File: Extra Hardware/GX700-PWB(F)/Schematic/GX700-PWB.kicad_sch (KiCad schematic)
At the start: 85 parts

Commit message: A lot of fixes.
Moved some libraries about to allow other schematics to share parts. 573 Expansion IO now has a proper symbol and part. JAE TX15 connector has a footprint. GX700 IO board has been fixed (output from chips was entirely wrong).
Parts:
- added CN31, CN32: 573_EXP, Connectors:JAE-TX15-80P, symbol Konami:573_EXP
- added H? (x3): MountingHole_Pad, symbol Mechanical:MountingHole_Pad
- added H?: MountingHole, symbol Mechanical:MountingHole
- added JP? (x3): Jumper_2_Open, symbol Jumper:Jumper_2_Open
- added RA2: 4.7k, Resistor_THT:R_Array_SIP9, symbol Device:R_Network08
- 10H: value (none) -> GAL16V8 (X700F1); footprint (none) -> Package_DIP:DIP-20_W7.62mm
- 3A: renamed from 6T?; value (none) -> PC817; footprint (none) -> Package_DIP:DIP-4_W7.62mm
- 3B: renamed from 6U?; value (none) -> PC817; footprint (none) -> Package_DIP:DIP-4_W7.62mm
- 3C: renamed from 6V?; value (none) -> PC817; footprint (none) -> Package_DIP:DIP-4_W7.62mm
- 3D: renamed from 6W?; value (none) -> PC817; footprint (none) -> Package_DIP:DIP-4_W7.62mm
- 3E, 3F, 3G, 3H, 3J, 3K, 3L, 3M, 3P, 3Q, 3R, 3S, 3T, 3U, 3V, 3W, 6T, 6U, 6V, 6W, 6X, 6Y, 6Z: value (none) -> PC817; footprint (none) -> Package_DIP:DIP-4_W7.62mm
- C17, C19, C6, C7, C8: value (none) -> 1uf; footprint (none) -> Capacitor_THT:C_Axial_L3.8mm_D2.6mm_P10.00mm_Horizontal
- C8: value (none) -> 1uf; footprint (none) -> 1uf
- CN33, CN34, CN35: value (none) -> B10PSHF1A; footprint (none) -> Connector_JST:JST_NH_B10P_SHD
- CN36: renamed from J?; value (none) -> B6PSHF1AA
- FL? (x28): value (none) -> EMI_Filter_LCL; footprint (none) -> Connector_PinSocket_2.54mm:PinSocket_1x03_P2.54mm_Vertical
- FL? (x4): value (none) -> EMI_Filter_LCL
- R11, R12, R13, R14: value (none) -> 4.7k; footprint (none) -> Resistor_THT:R_Axial_DIN0204_L3.6mm_D1.6mm_P5.08mm_Horizontal
- RA3: value (none) -> 4.7k; footprint (none) -> Resistor_THT:R_Array_SIP9
- RA4, RA5, RA?, RN6: value (none) -> 470; footprint (none) -> Resistor_THT:R_Array_SIP9
- U14, U3, U34: value (none) -> 74LS273; footprint (none) -> Package_DIP:DIP-20_W7.62mm
- U9: value (none) -> 74LS175; footprint (none) -> Package_DIP:DIP-16_W7.62mm
- U?: value (none) -> 74LS244
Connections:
- net +5V: now also CN31.a1 (+5V), CN31.a2 (+5V), CN31.a3 (+5V), CN31.a4 (+5V), CN31.a5 (+5V), CN31.b1 (+5V), CN31.b2 (+5V), CN31.b3 (+5V), CN31.b4 (+5V), CN31.b5 (+5V), CN32.a1 (+5V), CN32.a2 (+5V), CN32.a3 (+5V), CN32.a4 (+5V), CN32.a5 (+5V), CN32.b1 (+5V), CN32.b2 (+5V), CN32.b3 (+5V), CN32.b4 (+5V), CN32.b5 (+5V)
- net 573-D0: now also RA3.2 (R1), U?.17 (I3b), CN31.a32 (D0), CN32.a32 (D0); no longer RA3.9 (R8), U?.2 (I0a)
- net 573-D1: now also RA3.3 (R2), U?.15 (I2b), CN31.b32 (D1), CN32.b32 (D1); no longer RA3.8 (R7), U?.4 (I1a)
- net 573-D2: now also RA3.4 (R3), U?.13 (I1b), CN31.a31 (D2), CN32.a31 (D2); no longer RA3.7 (R6), U?.6 (I2a)
- net 573-D3: now also RA3.5 (R4), U?.11 (I0b), CN31.b31 (D3), CN32.b31 (D3); no longer RA3.6 (R5), U?.8 (I3a)
- net 573-D4: now also RA3.6 (R5), U?.8 (I3a), CN31.a30 (D4), CN32.a30 (D4); no longer RA3.5 (R4), U?.11 (I0b)
- net 573-D5: now also RA3.7 (R6), U?.6 (I2a), CN31.b30 (D5), CN32.b30 (D5); no longer RA3.4 (R3), U?.13 (I1b)
- net 573-D6: now also RA3.8 (R7), U?.4 (I1a), CN31.a29 (D6), CN32.a29 (D6); no longer RA3.3 (R2), U?.15 (I2b)
- net 573-D7: now also RA3.9 (R8), U?.2 (I0a), CN31.b29 (D7), CN32.b29 (D7); no longer RA3.2 (R1), U?.17 (I3b)
- net DATA-0: now also U?.3 (O3b); no longer U?.18 (O0a)
- net DATA-1: now also U?.5 (O2b); no longer U?.16 (O1a)
- net DATA-2: now also U?.7 (O1b); no longer U?.14 (O2a)
- net DATA-3: now also U?.9 (O0b); no longer U?.12 (O3a)
- net DATA-4: now also U?.12 (O3a); no longer U?.9 (O0b)
- net DATA-5: now also U?.14 (O2a); no longer U?.7 (O1b)
- net DATA-6: now also U?.16 (O1a); no longer U?.5 (O2b)
- net DATA-7: now also U?.18 (O0a); no longer U?.3 (O3b)
- net GND: now also CN31.a11 (GND), CN31.a13 (GND), CN31.a33 (GND), CN31.a34 (GND), CN31.a35 (GND), CN31.a8 (GND), CN31.a9 (GND), CN31.b11 (GND), CN31.b13 (GND), CN31.b33 (GND), CN31.b34 (GND), CN31.b35 (GND), CN31.b7 (GND), CN31.b9 (GND), CN32.a11 (GND), CN32.a13 (GND), CN32.a33 (GND), CN32.a34 (GND), CN32.a35 (GND), CN32.a8 (GND), CN32.a9 (GND), CN32.b11 (GND), CN32.b13 (GND), CN32.b33 (GND), CN32.b34 (GND), CN32.b35 (GND), CN32.b7 (GND), CN32.b9 (GND), JP?.1 (A), JP?.1 (A)
- net ISOLATED-COMMON: now also CN35.10 (Pin_10), CN36.6 (Pin_6), JP?.1 (A)
- net U14-CP: now also 10H.14 (IO6); no longer 10H.13 (IO7)
- net U3-CP: now also 10H.13 (IO7); no longer 10H.12 (IO8)
- net U34-CP: now also 10H.15 (IO5); no longer 10H.14 (IO6)
- net U9-CP: now also 10H.16 (IO4); no longer 10H.15 (IO5)
- net ~{RESET}: now also CN31.a10 (~{RESET}), CN32.a10 (~{RESET})
- net at U9.10 (Q2): now also 3B.2; no longer 3C.2
- net at U9.15 (Q3): now also 3A.2; no longer 3D.2
- net at U9.2 (Q0): now also 3D.2; no longer 3A.2
- net at U9.7 (Q1): now also 3C.2; no longer 3B.2
- net ~{EXP2}: now reaches 10H.1 (I1/CLK), R12.1
- net ~{EXP2}: now also CN31.a15 (~{EXP2}), CN32.a15 (~{EXP2})
- net ~{READ}: now reaches 10H.2 (I2), R14.1
- net ~{READ}: now also CN31.a6 (~{READ}), CN32.a6 (~{READ})
- net ~{WR1}: now reaches 10H.3 (I3), R11.1
- net ~{WR1}: now also CN31.b6 (~{WR1}), CN32.b6 (~{WR1})
- net at 3E.2: now also U34.19 (Q7); no longer U34.2 (Q0)
- net at CN35.1 (Pin_1), FL?.3: no longer CN35.10 (Pin_10)
- net at CN36.1 (Pin_1), FL?.3: no longer CN36.6 (Pin_6)
- net at U34.12 (Q4): now also 3L.2; no longer 3J.2
- net at U34.15 (Q5): now also 3J.2; no longer 3K.2
- net at U34.16 (Q6): now also 3G.2; no longer 3L.2
- net at 3M.2: now also U34.9 (Q3); no longer U34.19 (Q7)
- net at 3F.2: now also U34.2 (Q0); no longer U34.5 (Q1)
- net at U34.6 (Q2): now also 3K.2; no longer 3G.2
- net at 3H.2: now also U34.5 (Q1); no longer U34.9 (Q3)
- net at 3P.2: now also U14.19 (Q7); no longer U14.2 (Q0)
- net at U14.12 (Q4): now also 3V.2; no longer 3T.2
- net at U14.15 (Q5): now also 3T.2; no longer 3U.2
- net at U14.16 (Q6): now also 3R.2; no longer 3V.2
- net at 3W.2: now also U14.9 (Q3); no longer U14.19 (Q7)
- net at 3Q.2: now also U14.2 (Q0); no longer U14.5 (Q1)
- net at U14.6 (Q2): now also 3U.2; no longer 3R.2
- net at 3S.2: now also U14.5 (Q1); no longer U14.9 (Q3)
- net at 6T.2: now also U3.19 (Q7); no longer U3.2 (Q0)
- net at U3.12 (Q4): now also 6Y.2; no longer 6X.2
- net at U3.15 (Q5): now also 6X.2; no longer 6Y.2
- net at U3.16 (Q6): now also 6V.2; no longer 6Y.2
- net at 6Z.2: now also U3.9 (Q3); no longer U3.19 (Q7)
- net at 6U.2: now also U3.2 (Q0); no longer U3.5 (Q1)
- net at U3.6 (Q2): now also 6Y.2; no longer 6V.2
- net at 6W.2: now also U3.5 (Q1); no longer U3.9 (Q3)
- net 573-3V3 renamed +3V3
- net +3V3: now also CN31.a36 (+3V3), CN31.a37 (+3V3), CN31.a38 (+3V3), CN31.a39 (+3V3), CN31.a40 (+3V3), CN31.b36 (+3V3), CN31.b37 (+3V3), CN31.b38 (+3V3), CN31.b39 (+3V3), CN31.b40 (+3V3), CN32.a36 (+3V3), CN32.a37 (+3V3), CN32.a38 (+3V3), CN32.a39 (+3V3), CN32.a40 (+3V3), CN32.b36 (+3V3), CN32.b37 (+3V3), CN32.b38 (+3V3), CN32.b39 (+3V3), CN32.b40 (+3V3), RA2.1 (common)
- removed net 573-A??: 10H.5 (I5), 10H.6 (I6), 10H.7 (I7), 10H.8 (I8), 10H.9 (I9)
- new net: H?.1, JP?.2 (B) (x3)
- new net 573-A0: CN31.a24 (A0), CN32.a24 (A0)
- new net 573-A1: CN31.b24 (A1), CN32.b24 (A1)
- new net 573-A12: CN31.a20 (A12), CN32.a20 (A12)
- new net 573-A13: CN31.b20 (A13), CN32.b20 (A13)
- new net 573-A14: CN31.a19 (A14), CN32.a19 (A14)
- new net 573-A15: CN31.b19 (A15), CN32.b19 (A15)
- new net 573-A2: CN31.a23 (A2), CN32.a23 (A2)
- new net 573-A20: CN31.a18 (A20), CN32.a18 (A20)
- new net 573-A21: CN31.b18 (A21), CN32.b18 (A21)
- new net 573-A22: CN31.a17 (A22), CN32.a17 (A22)
- new net 573-A23: CN31.b17 (A23), CN32.b17 (A23)
- new net 573-A3: 10H.9 (I9), CN31.b23 (A3), CN32.b23 (A3), RA2.2 (R1)
- new net 573-A4: 10H.8 (I8), CN31.a22 (A4), CN32.a22 (A4), RA2.3 (R2)
- new net 573-A5: 10H.7 (I7), CN31.b22 (A5), CN32.b22 (A5), RA2.4 (R3)
- new net 573-A6: 10H.6 (I6), CN31.a21 (A6), CN32.a21 (A6), RA2.5 (R4)
- new net 573-A7: 10H.5 (I5), CN31.b21 (A7), CN32.b21 (A7), RA2.6 (R5)
- new net 573-D10: CN31.a27 (D10), CN32.a27 (D10)
- new net 573-D11: CN31.b27 (D11), CN32.b27 (D11)
- new net 573-D12: CN31.a26 (D12), CN32.a26 (D12)
- new net 573-D13: CN31.b26 (D13), CN32.b26 (D13)
- new net 573-D14: CN31.a25 (D14), CN32.a25 (D14)
- new net 573-D15: CN31.b25 (D15), CN32.b25 (D15)
- new net 573-D8: CN31.a28 (D8), CN32.a28 (D8)
- new net 573-D9: CN31.b28 (D9), CN32.b28 (D9)
- new net DREQ5: CN31.a14 (DREQ5), CN32.a14 (DREQ5)
- new net DREQ5-2: CN31.b12 (DREQ5), CN32.b12 (DREQ5)
- new net EXP-15: CN31.b15 (N/C), CN32.b15 (N/C)
- new net IRQ10: CN31.a16 (IRQ10), CN32.a16 (IRQ10)
- new net IRQ10-2: CN31.b16 (IRQ10), CN32.b16 (IRQ10)
- new net ~{EXP1-2}: CN31.b14 (~{EXP1}), CN32.b14 (~{EXP1})
- new net ~{EXP1}: CN31.a12 (~{EXP1}), CN32.a12 (~{EXP1})
- new net ~{RESET2}: CN31.b10 (~{RESET}), CN32.b10 (~{RESET})
- new net ~{WR2}: CN31.a7 (~{WR2}), CN32.a7 (~{WR2})
- no-connect marks 8 -> 15
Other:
- note added: "Connector 33"
- note added: "Connector CN34"
- note added: "Connector CN35"
- note added: "Connector CN36"
- note added: "Not populated (pass-thru?)"
- note added: "Not populated on DDR version"
- note added: "Not populayed on DDR IO board"
- note added: "On DDR this is the Player 1 pad CCFLs and CPLD data"
- note added: "On DDR this is the Player 2 pad CCFLs and Stage IO board data"
- note added: "On DDR this is the cab lighting output (Starts, marquee spots)"
- note removed: "On DDR this is the P1 pad ouput"
- note removed: "On DDR this is the P2 pad ouput"
- note removed: "On DDR this is the cabinet lighting ouput"
- moved on the sheet: 10H, 3A, 3B, 3C, 3D, 3E, 3F, 3G, 3H, 3J, 3K, 3L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

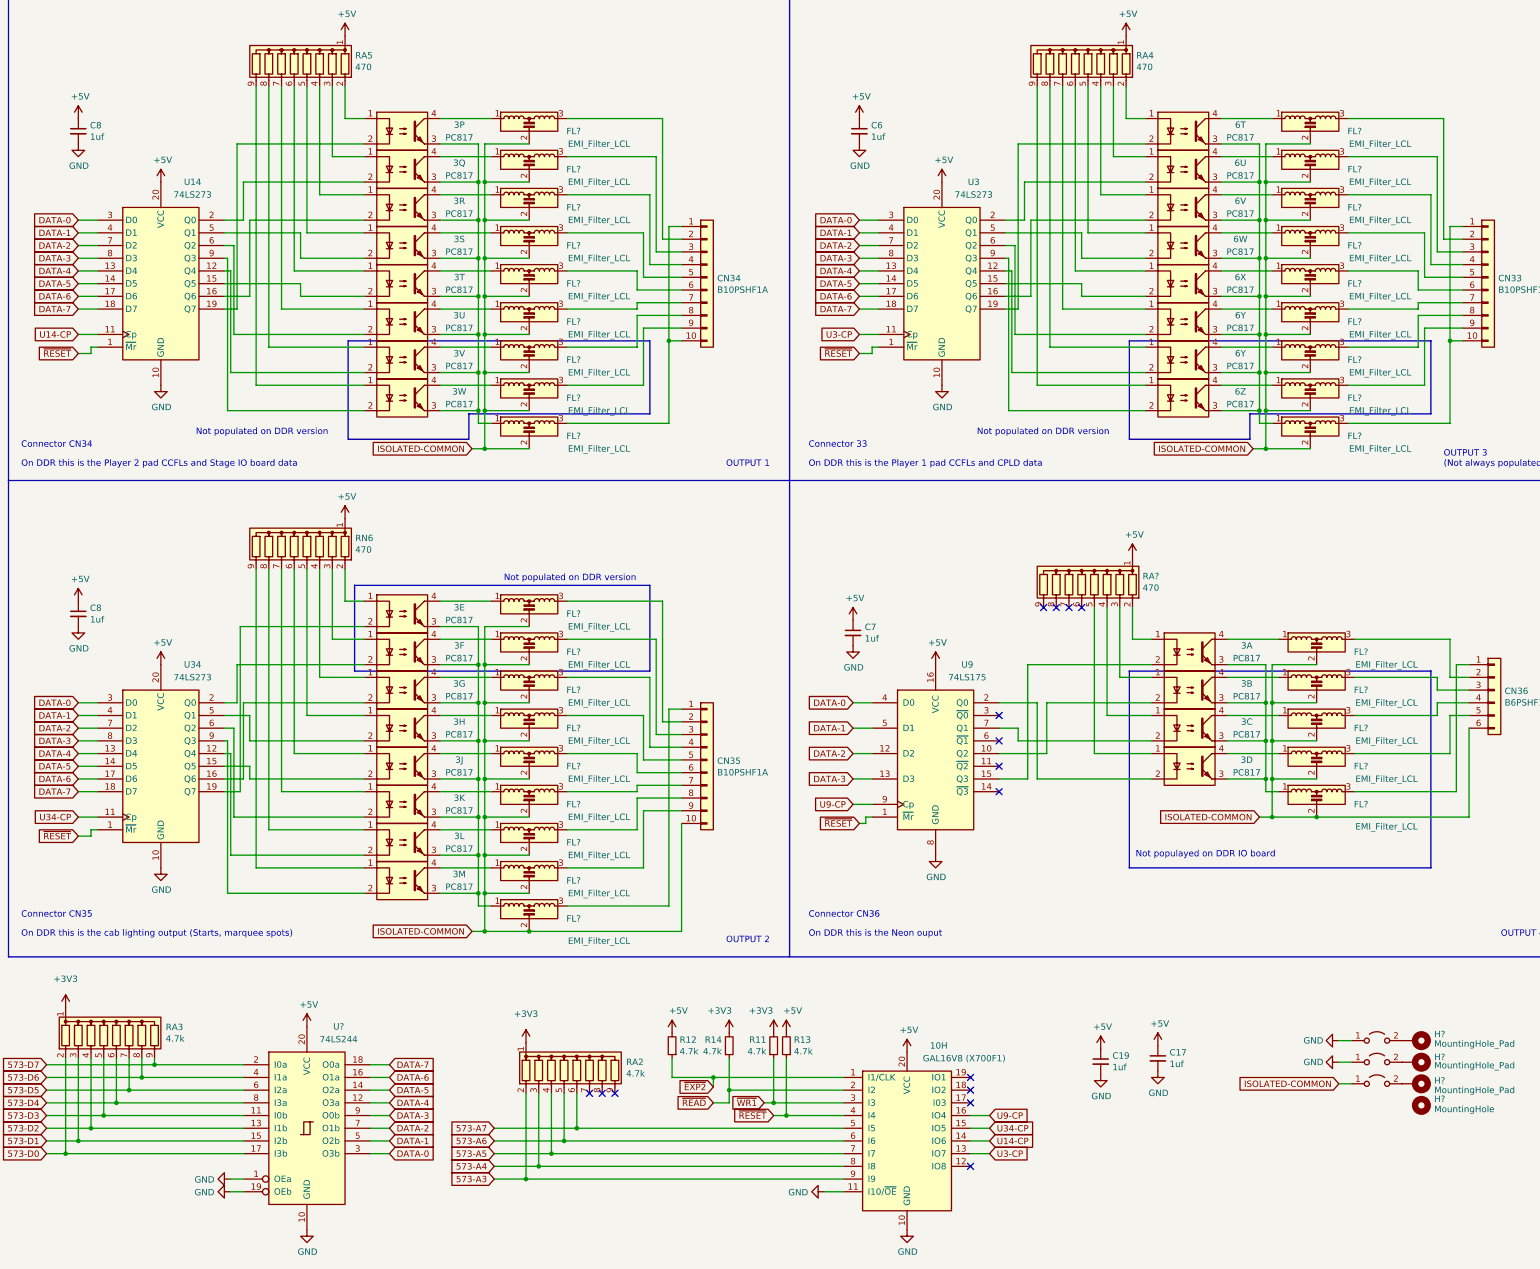
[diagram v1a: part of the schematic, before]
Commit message: Laid out GX700-PWB(F)
Needs traces doing but the measurements are all there.
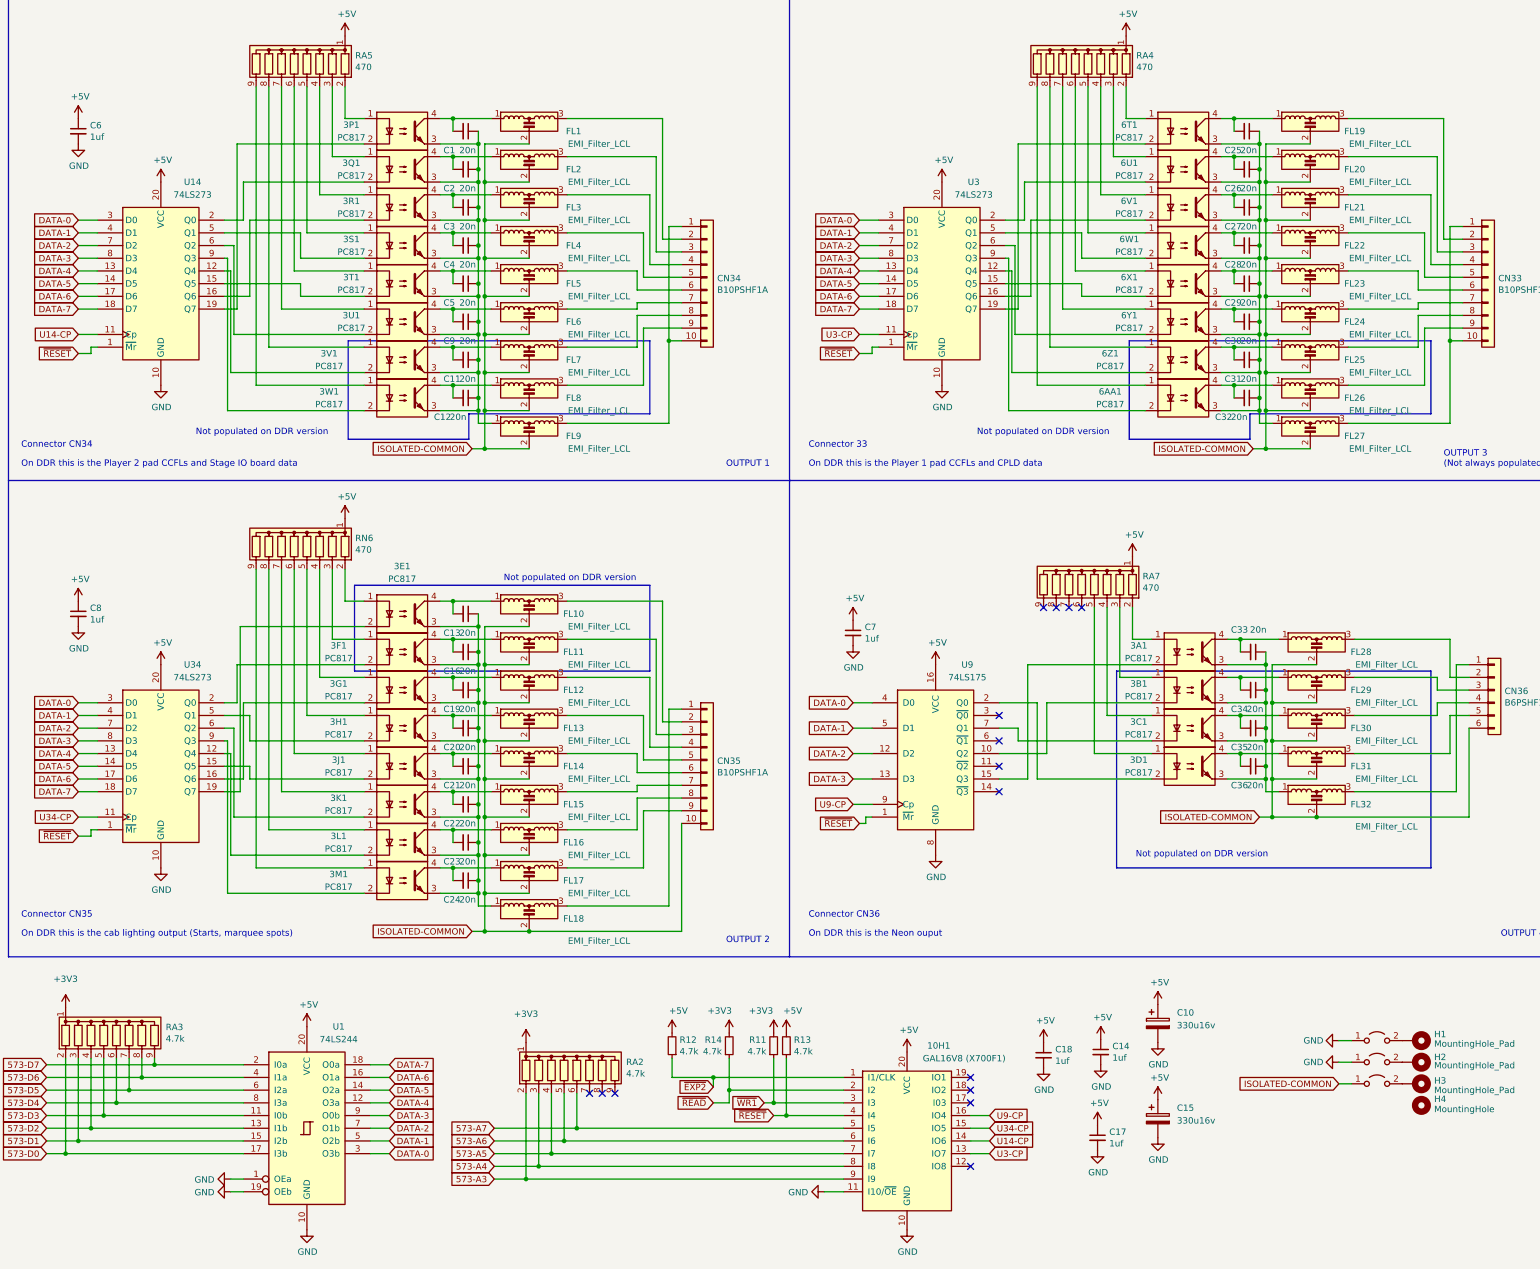
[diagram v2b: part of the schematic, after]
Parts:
- removed C6: 1uf, Capacitor_THT:C_Axial_L3.8mm_D2.6mm_P10.00mm_Horizontal, symbol Device:C_Small
- added C1, C11, C12, C13, C16, C19, C2, C20, C21, C22, C23, C24, C25, C26, C27, C28, C29, C3, C30, C31, C32, C33, C34, C35, C36, C4, C5, C9: 20n, Capacitor_THT:C_Axial_L3.8mm_D2.6mm_P7.50mm_Horizontal, symbol Device:C_Small
- added C10: 330u16v, Capacitor_THT:CP_Radial_D8.0mm_P3.50mm, symbol Device:C_Polarized
- added C15: 330u16v, Capacitor_THT:CP_Radial_D8.0mm_P2.50mm, symbol Device:C_Polarized
- added C17: 1uf, Capacitor_THT:C_Axial_L3.8mm_D2.6mm_P10.00mm_Horizontal, symbol Device:C_Small
- C8: footprint 1uf -> Capacitor_THT:C_Axial_L3.8mm_D2.6mm_P10.00mm_Horizontal
- CN33, CN34, CN35: footprint Connector_JST:JST_NH_B10P_SHD -> Connector_PinSocket_2.54mm:PinSocket_1x10_P2.54mm_Vertical
- CN36: footprint (none) -> Connector_PinSocket_2.54mm:PinSocket_1x06_P2.54mm_Vertical
- FL13, FL22, FL31, FL4: renamed from FL?; footprint (none) -> Connector_PinSocket_2.54mm:PinSocket_1x03_P2.54mm_Vertical
- H1, H2, H3: renamed from H?; footprint (none) -> MountingHole:MountingHole_3.5mm_Pad
- H4: renamed from H?; footprint (none) -> MountingHole:MountingHole_3.5mm
- JP1, JP2, JP3: renamed from JP?; footprint (none) -> Connector_PinSocket_2.54mm:PinSocket_1x02_P2.54mm_Vertical
- U1: renamed from U?; footprint (none) -> Package_DIP:DIP-20_W7.62mm
- gave numbers to parts that had none: 29
- renumbered 10H to 10H1, 3A to 3A1, 3B to 3B1, 3C to 3C1, 3D to 3D1, 3E to 3E1, 3F to 3F1, 3G to 3G1, 3H to 3H1, 3J to 3J1, 3K to 3K1, 3L to 3L1, 3M to 3M1, 3P to 3P1, 3Q to 3Q1, 3R to 3R1, 3S to 3S1, 3T to 3T1, 3U to 3U1, 3V to 3V1, 3W to 3W1, 6Z to 6AA1, 6T to 6T1, 6U to 6U1, 6V to 6V1, 6W to 6W1, 6X to 6X1, 6Y to 6Y1, 6Y to 6Z1, C17 to C14, C19 to C18, C8 to C6
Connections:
- net +5V: now also C10.1, C15.1, C17.1
- net GND: now also C10.2, C15.2, C17.2
- net at 3E1.3, 3F1.3, 3G1.3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: now also C13.1, C16.1, C19.1, C20.1, C21.1, C22.1, C23.1, C24.1
- net at 3E1.4, FL10.1: now also C13.2
- net at 3F1.4, FL11.1: now also C16.2
- net at 3G1.4, FL12.1: now also C19.2
- net at 3H1.4, FL13.1: now also C20.2
- net at 3J1.4, FL14.1: now also C21.2
- net at 3K1.4, FL15.1: now also C22.2
- net at 3L1.4, FL16.1: now also C23.2
- net at 3M1.4, FL17.1: now also C24.2
- net at 3P1.3, 3Q1.3, 3R1.3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: now also C1.1, C11.1, C12.1, C2.1, C3.1, C4.1, C5.1, C9.1
- net at 3P1.4, FL1.1: now also C1.2
- net at 3Q1.4, FL2.1: now also C2.2
- net at 3R1.4, FL3.1: now also C3.2
- net at 3S1.4, FL4.1: now also C4.2
- net at 3T1.4, FL5.1: now also C5.2
- net at 3U1.4, FL6.1: now also C9.2
- net at 3V1.4, FL7.1: now also C11.2
- net at 3W1.4, FL8.1: now also C12.2
- net at 6AA1.3, 6T1.3, 6U1.3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: now also C25.1, C26.1, C27.1, C28.1, C29.1, C30.1, C31.1, C32.1
- net at 6T1.4, FL19.1: now also C25.2
- net at 6U1.4, FL20.1: now also C26.2
- net at 6V1.4, FL21.1: now also C27.2
- net at 6W1.4, FL22.1: now also C28.2
- net at 6X1.4, FL23.1: now also C29.2
- net at 6Y1.4, FL24.1: now also C30.2
- net at 6Z1.4, FL25.1: now also C31.2
- net at 6AA1.4, FL26.1: now also C32.2
- net at 3A1.3, 3B1.3, 3C1.3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: now also C33.1, C34.1, C35.1, C36.1
- net at 3A1.4, FL28.1: now also C33.2
- net at 3B1.4, FL29.1: now also C34.2
- net at 3C1.4, FL30.1: now also C35.2
- net at 3D1.4, FL31.1: now also C36.2
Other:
- note removed: "Not populayed on DDR IO board"
- moved on the sheet: C14, C18
